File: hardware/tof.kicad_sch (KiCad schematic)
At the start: 5 parts, among them U5 VL53L1CXV0FY1

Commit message: feat(kicad): Cleared ERC errors and assigned footprints for all parts
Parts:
- C24: footprint (none) -> Capacitor_SMD:C_0402_1005Metric
- C25: footprint (none) -> Capacitor_SMD:C_0603_1608Metric
- R16, R17: footprint (none) -> Resistor_SMD:R_0402_1005Metric
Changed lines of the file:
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@@
 			)
 		)
-		(property "Footprint" ""
+		(property "Footprint" "Resistor_SMD:R_0402_1005Metric"
 			(at 131.318 69.85 90)
 			(hide yes)
@@
 			)
 		)
-		(property "Footprint" ""
+		(property "Footprint" "Capacitor_SMD:C_0402_1005Metric"
 			(at 154.94 61.2648 0)
 			(hide yes)
@@
 			)
 		)
-		(property "Footprint" ""
+		(property "Footprint" "Resistor_SMD:R_0402_1005Metric"
 			(at 125.222 69.85 90)
 			(hide yes)
@@
 			)
 		)
-		(property "Footprint" ""
+		(property "Footprint" "Capacitor_SMD:C_0603_1608Metric"
 			(at 154.94 66.3448 0)
 			(hide yes)

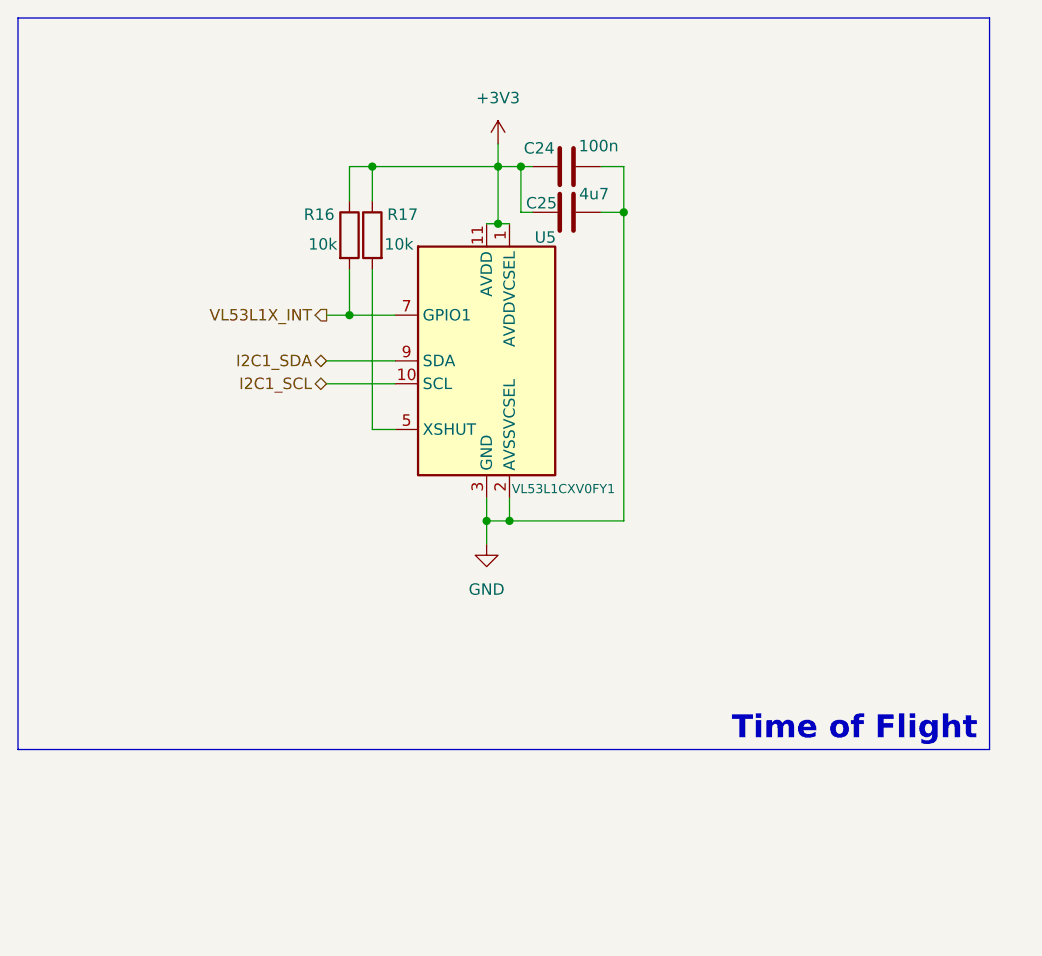
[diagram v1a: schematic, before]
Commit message: feat(kicad): Added VL53l10x application notes
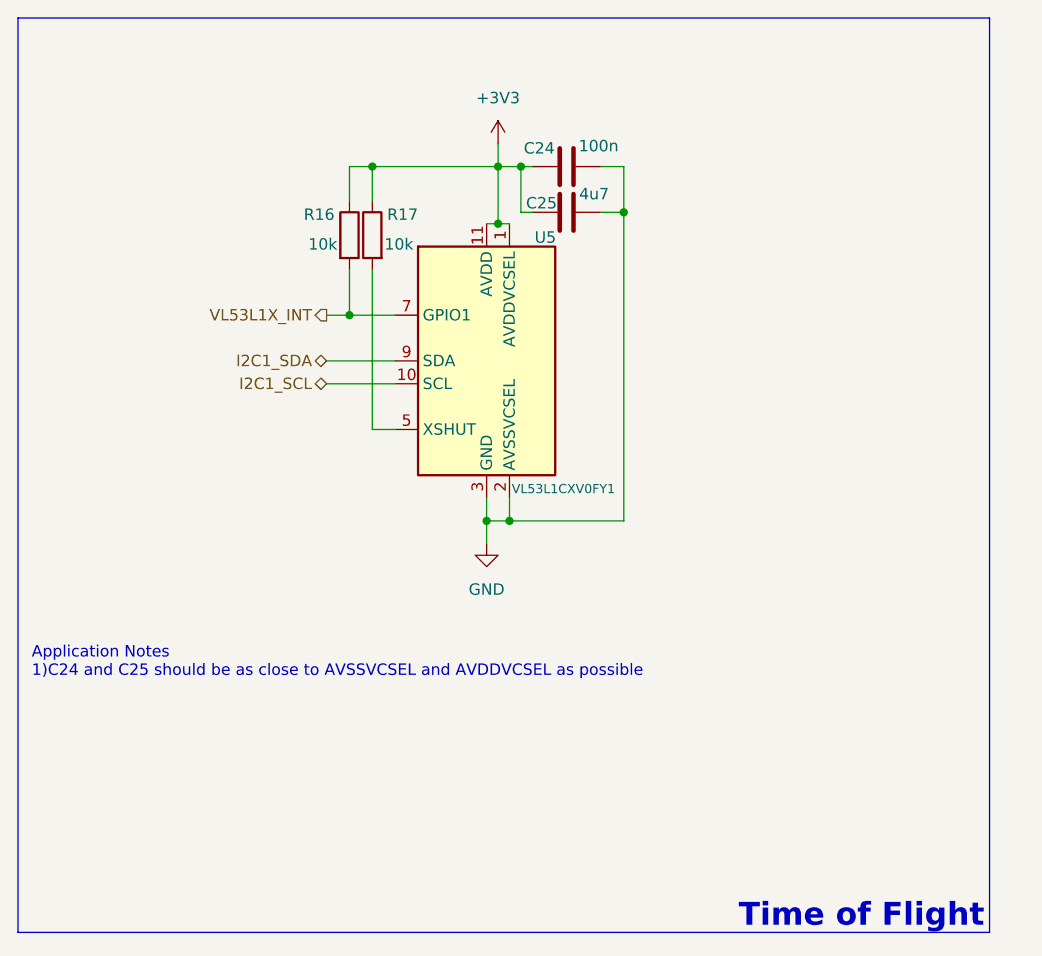
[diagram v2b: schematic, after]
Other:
- note added: "Application Notes 1)C24 and C25 should be as close to AVSSVCSEL and AVDDVCSEL as possible"
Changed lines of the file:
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@@
 	(rectangle
 		(start 90.17 45.72)
-		(end 198.12 127)
+		(end 198.12 147.32)
 		(stroke
 			(width 0)
@@
 		)
 	)
+	(text "Application Notes\n1)C24 and C25 should be as close to AVSSVCSEL and AVDDVCSEL as possible"
+		(exclude_from_sim no)
+		(at 91.694 117.348 0)
+		(effects
+			(font
+				(size 1.27 1.27)
+			)
+			(justify left)
+		)
+	)
 	(text "Time of Flight\n"
 		(exclude_from_sim no)
-		(at 183.134 124.714 0)
+		(at 183.896 145.542 0)
 		(effects
 			(font

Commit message: feat(kicad): Routing complete, assigning jlc components to each footprint
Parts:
- C24: LCSC (none) -> C1525
- R16, R17: LCSC (none) -> C25744
- U5: LCSC (none) -> C190004
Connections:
- net VL53L1X_XSHUT: now reaches R17.2, U5.5 (XSHUT)
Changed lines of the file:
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@@
+		)
+	)
+	(hierarchical_label "VL53L1X_XSHUT"
+		(shape input)
+		(at 129.54 91.44 180)
+		(effects
+			(font
+				(size 1.27 1.27)
+			)
+			(justify right)
 		)
 	)
@@
 			)
 		)
+		(property "LCSC" "C25744"
+			(at 129.54 69.85 0)
+			(hide yes)
+			(show_name no)
+			(do_not_autoplace no)
+			(effects
+				(font
+					(size 1.27 1.27)
+				)
+			)
+		)
+		(property "KLC_S3.3" ""
+			(at 129.54 69.85 0)
+			(hide yes)
+			(show_name no)
+			(do_not_autoplace no)
+			(effects
+				(font
+					(size 1.27 1.27)
+				)
+			)
+		)
+		(property "KLC_S4.1" ""
+			(at 129.54 69.85 0)
+			(hide yes)
+			(show_name no)
+			(do_not_autoplace no)
+			(effects
+				(font
+					(size 1.27 1.27)
+				)
+			)
+		)
 		(pin "1"
 		)
@@
 		(property "Description" "Unpolarized capacitor"
 			(at 151.13 62.23 0)
+			(hide yes)
+			(show_name no)
+			(do_not_autoplace no)
+			(effects
+				(font
+					(size 1.27 1.27)
+				)
+			)
+		)
+		(property "LCSC" "C1525"
+			(at 151.13 62.23 90)
+			(hide yes)
+			(show_name no)
+			(do_not_autoplace no)
+			(effects
+				(font
+					(size 1.27 1.27)
+				)
+			)
+		)
+		(property "KLC_S3.3" ""
+			(at 151.13 62.23 90)
+			(hide yes)
+			(show_name no)
+			(do_not_autoplace no)
+			(effects
+				(font
+					(size 1.27 1.27)
+				)
+			)
+		)
+		(property "KLC_S4.1" ""
+			(at 151.13 62.23 90)
 			(hide yes)
 			(show_name no)
@@
 			)
 		)
+		(property "LCSC" "C25744"
+			(at 127 69.85 0)
+			(hide yes)
+			(show_name no)
+			(do_not_autoplace no)
+			(effects
+				(font
+					(size 1.27 1.27)
+				)
+			)
+		)
+		(property "KLC_S3.3" ""
+			(at 127 69.85 0)
+			(hide yes)
+			(show_name no)
+			(do_not_autoplace no)
+			(effects
+				(font
+					(size 1.27 1.27)
+				)
+			)
+		)
+		(property "KLC_S4.1" ""
+			(at 127 69.85 0)
+			(hide yes)
+			(show_name no)
+			(do_not_autoplace no)
+			(effects
+				(font
+					(size 1.27 1.27)
+				)
+			)
+		)
 		(pin "1"
 		)
@@
 			)
 		)
+		(property "LCSC" ""
+			(at 151.13 67.31 90)
+			(hide yes)
+			(show_name no)
+			(do_not_autoplace no)
+			(effects
+				(font
+					(size 1.27 1.27)
+				)
+			)
+		)
+		(property "KLC_S3.3" ""
+			(at 151.13 67.31 90)
+			(hide yes)
+			(show_name no)
+			(do_not_autoplace no)
+			(effects
+				(font
+					(size 1.27 1.27)
+				)
+			)
+		)
+		(property "KLC_S4.1" ""
+			(at 151.13 67.31 90)
+			(hide yes)
+			(show_name no)
+			(do_not_autoplace no)
+			(effects
+				(font
+					(size 1.27 1.27)
+				)
+			)
+		)
 		(pin "2"
 		)
@@
 			(at 142.24 83.82 0)
 			(hide yes)
+			(show_name no)
+			(do_not_autoplace no)
+			(effects
+				(font
+					(size 1.27 1.27)
+				)
+			)
+		)
+		(property "LCSC" "C190004 "
+			(at 142.24 83.82 0)
+			(hide yes)
+			(show_name no)
+			(do_not_autoplace no)
+			(effects
+				(font
+					(size 1.27 1.27)
+				)
+			)
+		)
+		(property "KLC_S3.3" ""
+			(at 142.24 83.82 0)
+			(hide yes)
+			(show_name no)
+			(do_not_autoplace no)
+			(effects
+				(font
+					(size 1.27 1.27)
+				)
+			)
+		)
+		(property "KLC_S4.1" ""
+			(at 142.24 83.82 0)
+			(hide yes)

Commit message: feat(kicad): Cleaned up routing and picked LCSC parts for several components
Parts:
- C25: LCSC (none) -> C19666
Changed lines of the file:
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@@
 			)
 		)
-		(property "LCSC" ""
+		(property "LCSC" "C19666"
 			(at 151.13 67.31 90)
 			(hide yes)
